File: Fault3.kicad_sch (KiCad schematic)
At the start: 26 parts

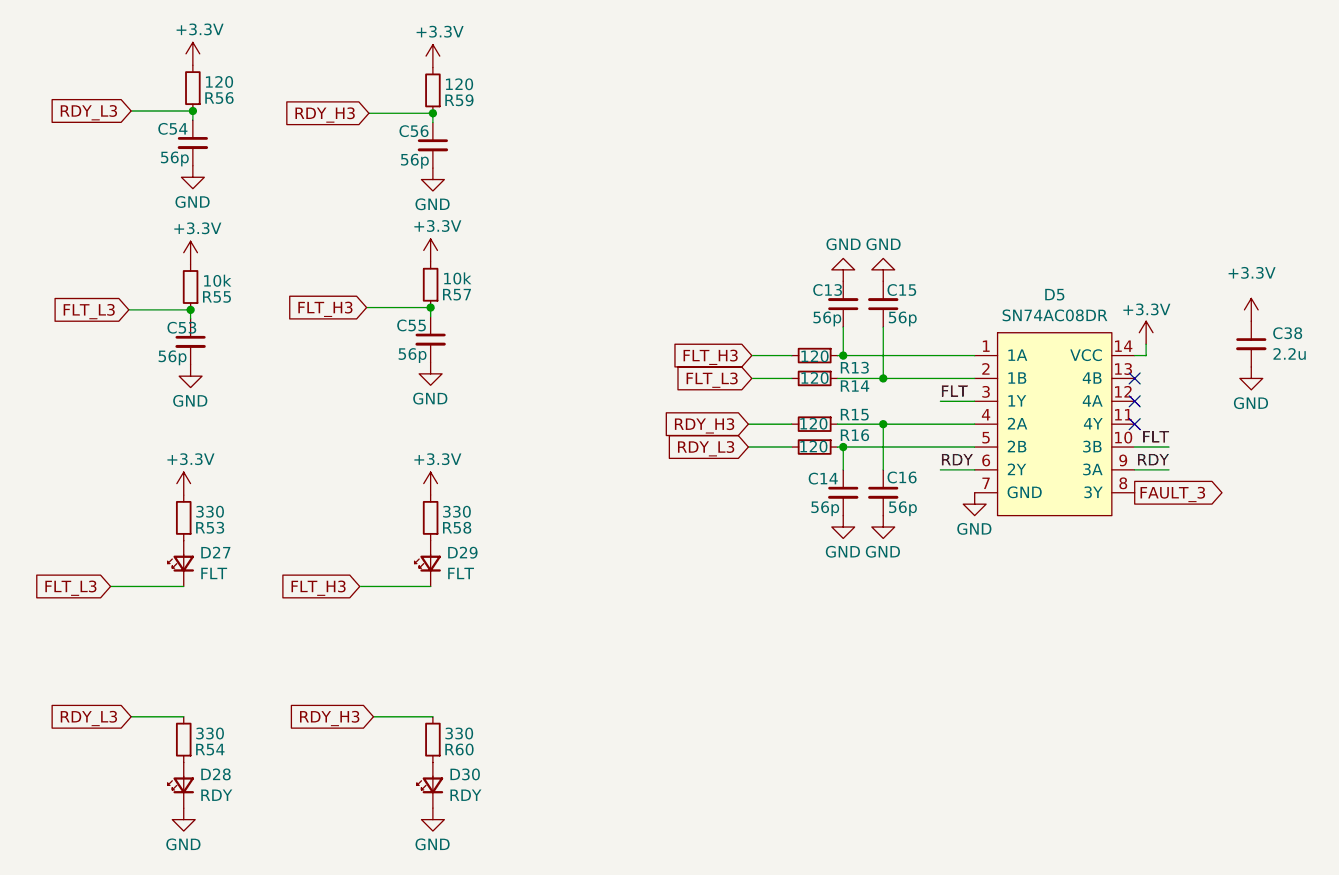
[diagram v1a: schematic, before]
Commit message: Изменил схему
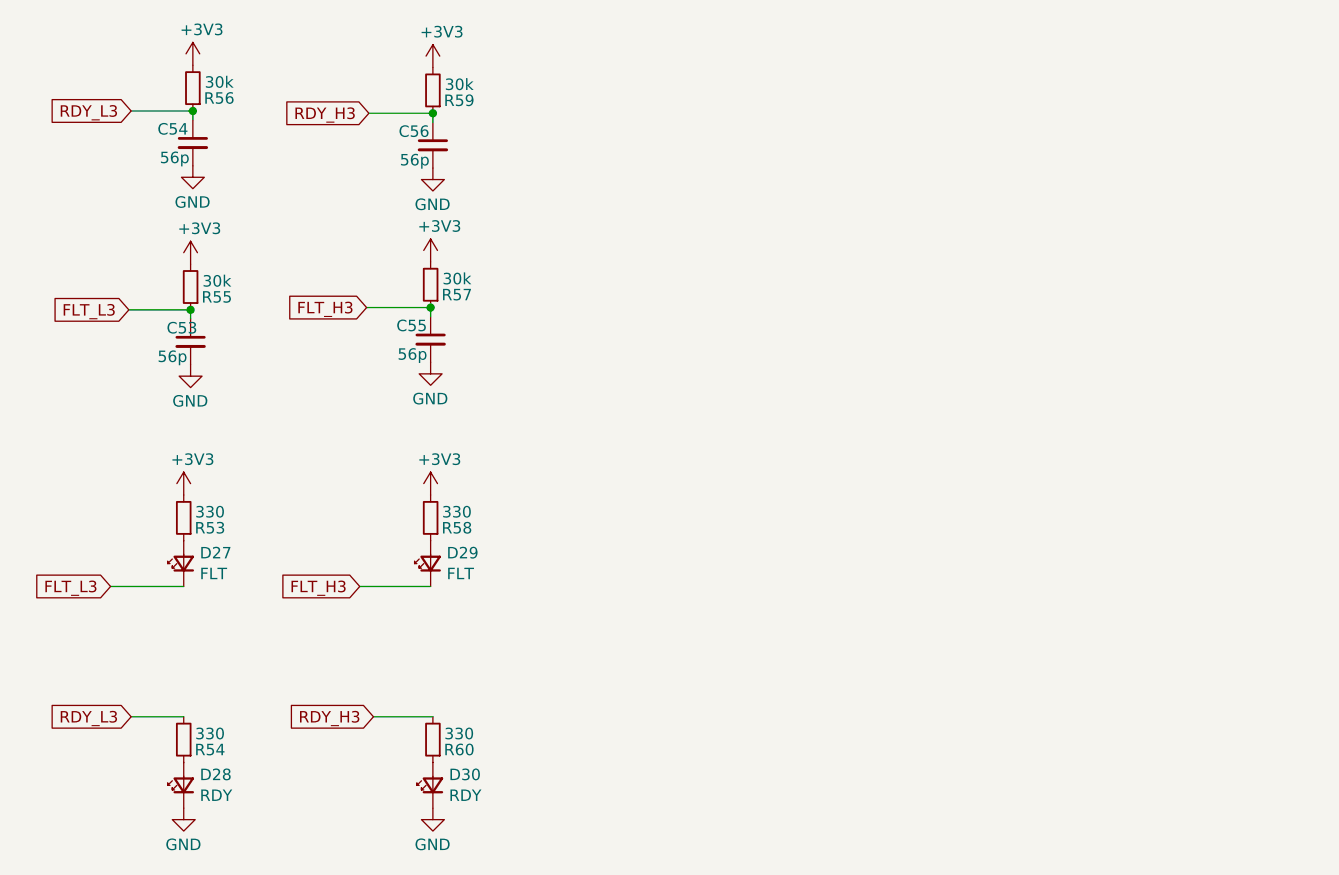
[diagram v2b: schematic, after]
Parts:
- removed C13, C14, C15, C16: 56p, Capacitor_SMD:C_0805_2012Metric_Pad1.18x1.45mm_HandSolder, symbol Device:C_Small
- removed C38: 2.2u, Capacitor_SMD:C_0805_2012Metric_Pad1.18x1.45mm_HandSolder, symbol Device:C_Small
- removed D5: SN74AC08DR, Package_SO:SOIC-14_3.9x8.7mm_P1.27mm, symbol Logic:SN74AC08DR
- removed R13, R14, R15, R16: 120, Resistor_SMD:R_0805_2012Metric_Pad1.20x1.40mm_HandSolder, symbol Device:R_Small
- R55, R57: value 10k -> 30k
- R56, R59: value 120 -> 30k
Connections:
- no-connect marks 3 -> 0
